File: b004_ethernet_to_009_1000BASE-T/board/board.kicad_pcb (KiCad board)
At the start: 2 copper layers, 21 x 29 mm, 8 parts, among them J1 009_1000BASE-T_2x5, J2 011_GPIO_2x3, J3 PoE_2x2, U1 7499211121A

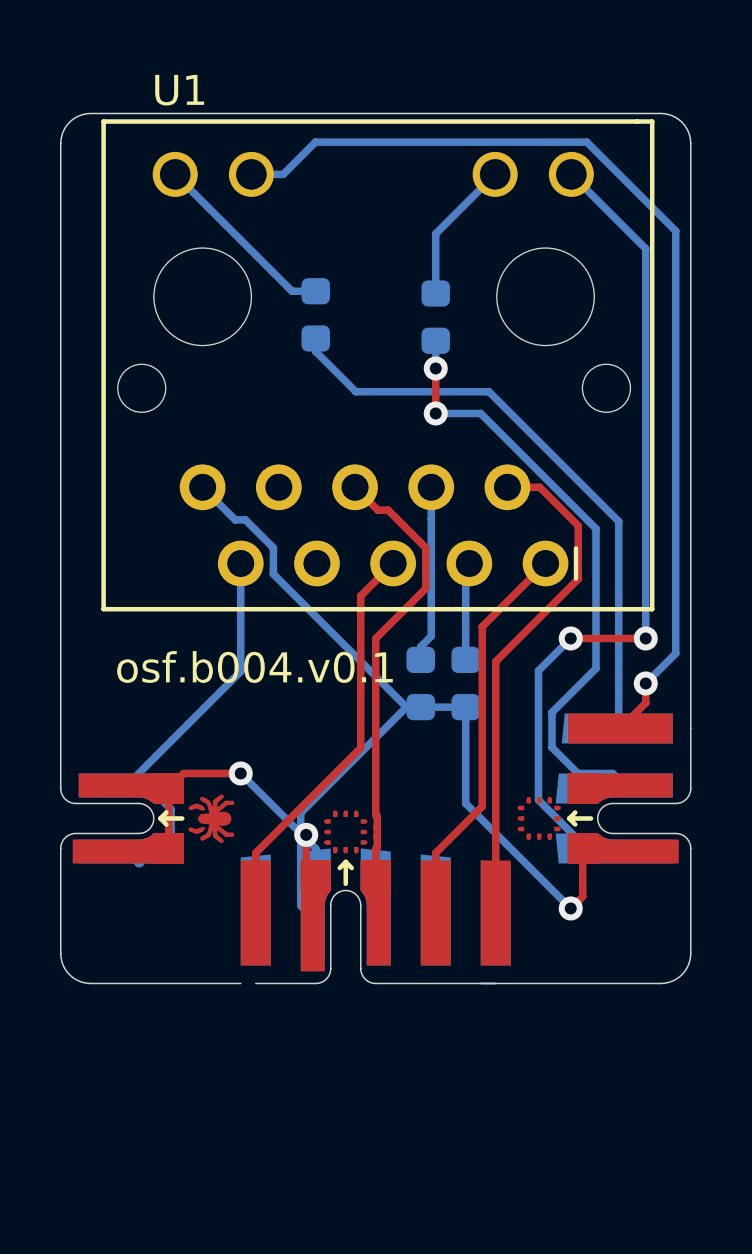
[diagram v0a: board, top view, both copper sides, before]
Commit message: added part info for silicon parts
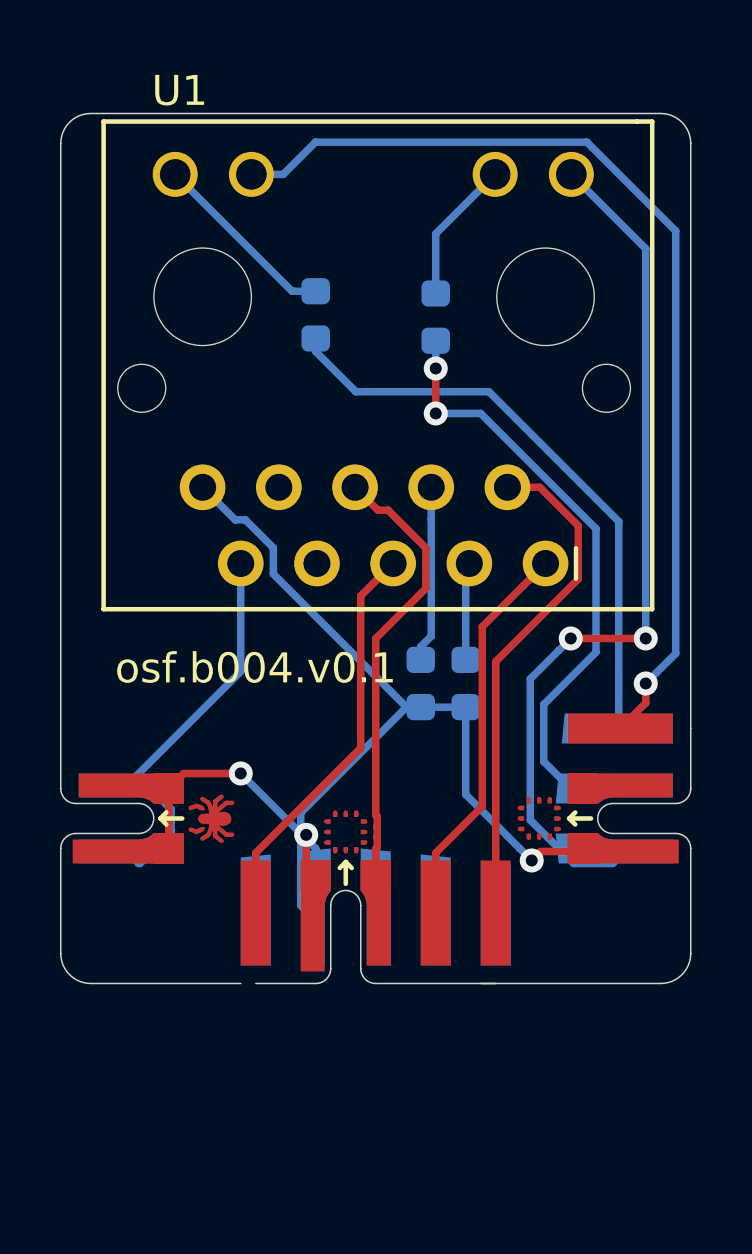
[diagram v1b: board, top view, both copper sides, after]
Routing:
- net GND: track 46.4 -> 44.0 mm
- net Net-(J2-Pad3): track 28.5 -> 29.7 mm
- net Net-(J2-Pad4): track 20.3 -> 21.0 mm
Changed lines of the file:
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@@
     (thickness 1.6)
     (drawings 12)
-    (tracks 110)
+    (tracks 113)
     (zones 0)
     (modules 8)
@@
   (gr_line (start 91 70) (end 110 70) (layer Edge.Cuts) (width 0.05))
   (segment (start 102 89.7875) (end 103.5 89.7875) (width 0.25) (layer B.Cu) (net 1))
-  (via (at 107 96.5) (size 0.8) (drill 0.4) (layers F.Cu B.Cu) (net 1))
-  (segment (start 107.4 94.5) (end 107.4 96.1) (width 0.25) (layer F.Cu) (net 1))
-  (segment (start 107.4 96.1) (end 107 96.5) (width 0.25) (layer F.Cu) (net 1))
-  (segment (start 103.5 93) (end 103.5 89.7875) (width 0.25) (layer B.Cu) (net 1))
-  (segment (start 107 96.5) (end 103.5 93) (width 0.25) (layer B.Cu) (net 1))
   (segment (start 98 93.3125) (end 101.525 89.7875) (width 0.25) (layer B.Cu) (net 1))
   (segment (start 98 96.4) (end 98 93.3125) (width 0.25) (layer B.Cu) (net 1))
@@
   (segment (start 95.817001 83.547001) (end 96.155763 83.547001) (width 0.25) (layer B.Cu) (net 1))
   (segment (start 94.73 82.46) (end 95.817001 83.547001) (width 0.25) (layer B.Cu) (net 1))
+  (via (at 105.7 94.900002) (size 0.8) (drill 0.4) (layers F.Cu B.Cu) (net 1))
+  (segment (start 103.5 89.7875) (end 103.5 92.700002) (width 0.25) (layer B.Cu) (net 1))
+  (segment (start 103.5 92.700002) (end 105.300001 94.500003) (width 0.25) (layer B.Cu) (net 1))
+  (segment (start 105.300001 94.500003) (end 105.7 94.900002) (width 0.25) (layer B.Cu) (net 1))
+  (segment (start 106.000002 94.6) (end 105.7 94.900002) (width 0.25) (layer F.Cu) (net 1))
+  (segment (start 107.4 94.5) (end 107.3 94.6) (width 0.25) (layer F.Cu) (net 1))
+  (segment (start 107.3 94.6) (end 106.000002 94.6) (width 0.25) (layer F.Cu) (net 1))
   (segment (start 100.5 94.515699) (end 100.5 95.4) (width 0.25) (layer F.Cu) (net 2))
   (segment (start 100.55001 94.134311) (end 100.55001 94.465689) (width 0.25) (layer F.Cu) (net 2))
@@
   (segment (start 104.5 88.268762) (end 104.5 96.65) (width 0.25) (layer F.Cu) (net 7))
   (segment (start 104.89 82.46) (end 105.96763 82.46) (width 0.25) (layer F.Cu) (net 7))
-  (segment (start 106.37499 89.965376) (end 107.840366 88.5) (width 0.25) (layer B.Cu) (net 8))
-  (segment (start 106.37499 91.134626) (end 106.37499 89.965376) (width 0.25) (layer B.Cu) (net 8))
-  (segment (start 107.240364 92) (end 106.37499 91.134626) (width 0.25) (layer B.Cu) (net 8))
-  (segment (start 108.9 92.5) (end 108.4 92) (width 0.25) (layer B.Cu) (net 8))
-  (segment (start 108.4 92) (end 107.240364 92) (width 0.25) (layer B.Cu) (net 8))
-  (segment (start 107.840366 88.5) (end 107.840366 83.840366) (width 0.25) (layer B.Cu) (net 8))
-  (segment (start 104 80) (end 102.5 80) (width 0.25) (layer B.Cu) (net 8))
-  (segment (start 107.840366 83.840366) (end 104 80) (width 0.25) (layer B.Cu) (net 8))
   (via (at 102.5 80) (size 0.8) (drill 0.4) (layers F.Cu B.Cu) (net 8))
   (via (at 102.5 78.5) (size 0.8) (drill 0.4) (layers F.Cu B.Cu) (net 8))
   (segment (start 102.5 80) (end 102.5 78.5) (width 0.25) (layer F.Cu) (net 8))
   (segment (start 102.5 78.5) (end 102.5 77.575) (width 0.25) (layer B.Cu) (net 8))
+  (segment (start 104 80) (end 102.5 80) (width 0.25) (layer B.Cu) (net 8))
+  (segment (start 107.840366 83.840366) (end 104 80) (width 0.25) (layer B.Cu) (net 8))
+  (segment (start 107 92.5) (end 106.1 91.6) (width 0.25) (layer B.Cu) (net 8))
+  (segment (start 108.9 92.5) (end 107 92.5) (width 0.25) (layer B.Cu) (net 8))
+  (segment (start 106.1 89.7) (end 107.840366 87.959634) (width 0.25) (layer B.Cu) (net 8))
+  (segment (start 106.1 91.6) (end 106.1 89.7) (width 0.25) (layer B.Cu) (net 8))
+  (segment (start 107.840366 87.959634) (end 107.840366 83.840366) (width 0.25) (layer B.Cu) (net 8))
   (via (at 107 87.5) (size 0.8) (drill 0.4) (layers F.Cu B.Cu) (net 9))
-  (segment (start 105.924979 88.575021) (end 107 87.5) (width 0.25) (layer B.Cu) (net 9))
-  (segment (start 105.924979 92.884615) (end 105.924979 88.575021) (width 0.25) (layer B.Cu) (net 9))
-  (segment (start 108.9 94.5) (end 107.540364 94.5) (width 0.25) (layer B.Cu) (net 9))
-  (segment (start 107.540364 94.5) (end 105.924979 92.884615) (width 0.25) (layer B.Cu) (net 9))
   (via (at 109.5 87.5) (size 0.8) (drill 0.4) (layers F.Cu B.Cu) (net 9))
   (segment (start 107 87.5) (end 109.5 87.5) (width 0.25) (layer F.Cu) (net 9))
   (segment (start 109.5 74.51) (end 107.02 72.03) (width 0.25) (layer B.Cu) (net 9))
   (segment (start 109.5 87.5) (end 109.5 74.51) (width 0.25) (layer B.Cu) (net 9))
+  (segment (start 108.9 94.5) (end 108.4 95) (width 0.25) (layer B.Cu) (net 9))
+  (segment (start 108.4 95) (end 107.1 95) (width 0.25) (layer B.Cu) (net 9))
+  (segment (start 105.649989 88.850011) (end 106.600001 87.899999) (width 0.25) (layer B.Cu) (net 9))
+  (segment (start 106.600001 87.899999) (end 107 87.5) (width 0.25) (layer B.Cu) (net 9))
+  (segment (start 107.1 95) (end 105.649989 93.549989) (width 0.25) (layer B.Cu) (net 9))
+  (segment (start 105.649989 93.549989) (end 105.649989 88.850011) (width 0.25) (layer B.Cu) (net 9))
   (segment (start 99.837498 79.274998) (end 98.5 77.9375) (width 0.25) (layer B.Cu) (net 10))
   (segment (start 98.5 77.9375) (end 98.5 77.5) (width 0.25) (layer B.Cu) (net 10))

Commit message: updated b004 to use version 0.2 connectors
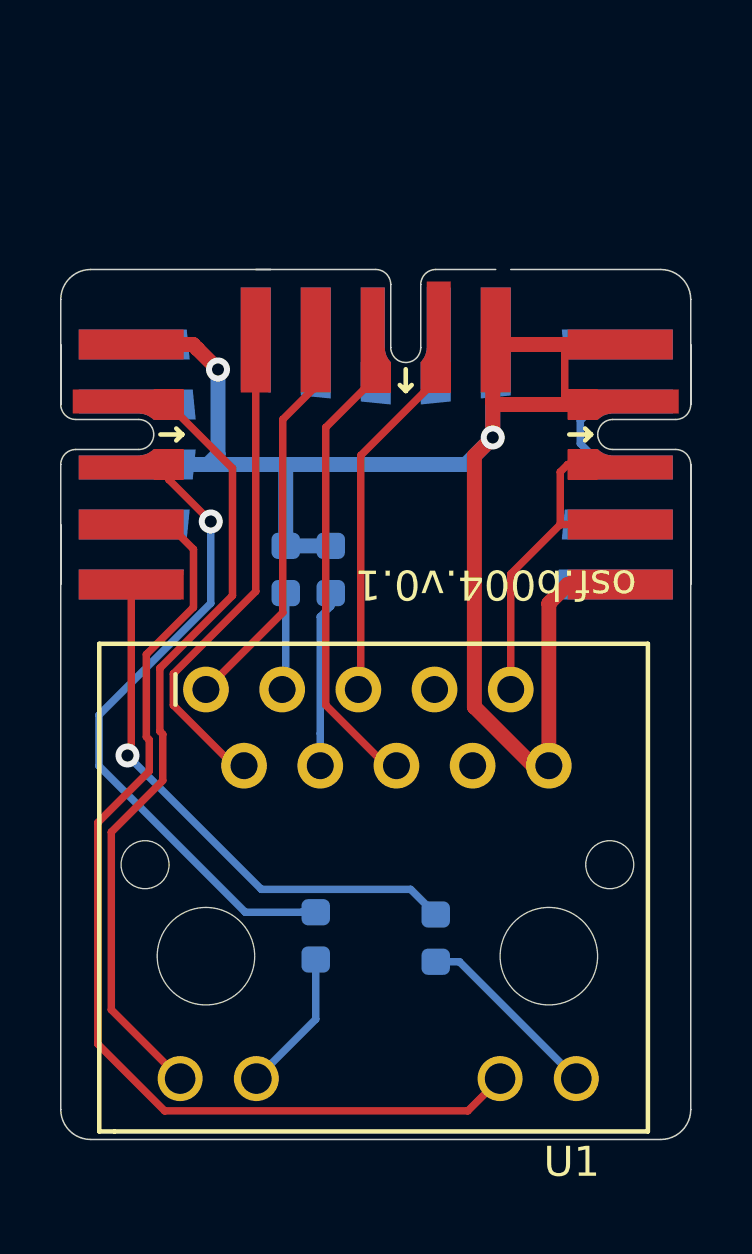
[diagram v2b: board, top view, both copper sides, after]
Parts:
- J2: footprint on_edge:on_edge_2x03_device -> on_edge:on_edge_2x05_device
- J3: footprint on_edge:on_edge_2x02_host -> on_edge:on_edge_2x05_host
- moved J1 23.8 mm to (100.5, 75.2), turned to 180 degrees
- moved J2 23.6 mm to (90.0, 81.7), turned to 270 degrees
- moved J3 23.6 mm to (111.0, 81.7), turned to 270 degrees
- moved R1 21.2 mm to (102.5, 97.5), turned to 90 degrees
- moved R2 21.0 mm to (98.5, 97.4), turned to 90 degrees
- moved U1 9.93 mm to (105.0, 89.2), turned to 180 degrees
- moved C1 7.10 mm to (97.5, 85.2), turned to 90 degrees
- moved C2 4.84 mm to (99.0, 85.2), turned to 90 degrees
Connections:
- J1 pad 3: GND -> Net-(J1-Pad3)
- J1 pad 4: (no net) -> Net-(J1-Pad4)
- J1 pad 6: (no net) -> GND
- J1 pad 7: Net-(J1-Pad7) -> (no net)
- J1 pad 9: Net-(J1-Pad9) -> (no net)
- J2 pad 2: (no net) -> Net-(J2-Pad2)
- J2 pad 6: Net-(J2-Pad6) -> (no net)
- R1 pad 2: Net-(J2-Pad6) -> Net-(J2-Pad5)
- R2 pad 2: Net-(J2-Pad4) -> Net-(J2-Pad3)
- U1 pad 1: Net-(J1-Pad5) -> Net-(J1-Pad4)
- U1 pad 11: Net-(J2-Pad3) -> Net-(J2-Pad2)
- U1 pad 13: Net-(J2-Pad5) -> Net-(J2-Pad4)
- U1 pad 2: Net-(J1-Pad9) -> Net-(J1-Pad5)
- U1 pad 5: Net-(J1-Pad7) -> Net-(J1-Pad2)
- U1 pad 6: Net-(J1-Pad2) -> Net-(J1-Pad3)
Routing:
- net Net-(J2-Pad2): track 0.00 -> 26.1 mm
- net GND: track 44.0 -> 64.8 mm, vias 3 -> 2
- net Net-(J2-Pad6): track 19.8 -> 0.00 mm
- net Net-(J1-Pad9): track 16.9 -> 0.00 mm
- net Net-(J2-Pad5): track 33.2 -> 18.2 mm
- net Net-(J1-Pad3): track 0.00 -> 14.8 mm
- net Net-(J2-Pad4): track 21.0 -> 35.1 mm, vias 2 -> 0
- net Net-(J1-Pad7): track 13.5 -> 0.00 mm
- net Net-(J1-Pad4): track 0.00 -> 13.2 mm
- net Net-(J2-Pad3): track 29.7 -> 21.4 mm, vias 2 -> 1
- net (no net): track 0.00 -> 4.69 mm
- net Net-(J1-Pad2): track 14.9 -> 11.5 mm
- net Net-(J1-Pad5): track 13.2 -> 16.5 mm
- net Net-(J3-Pad3): track 14.0 -> 10.8 mm
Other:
- outline, holes or cut-outs redrawn

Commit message: changed connector to include 100BASE-T center taps
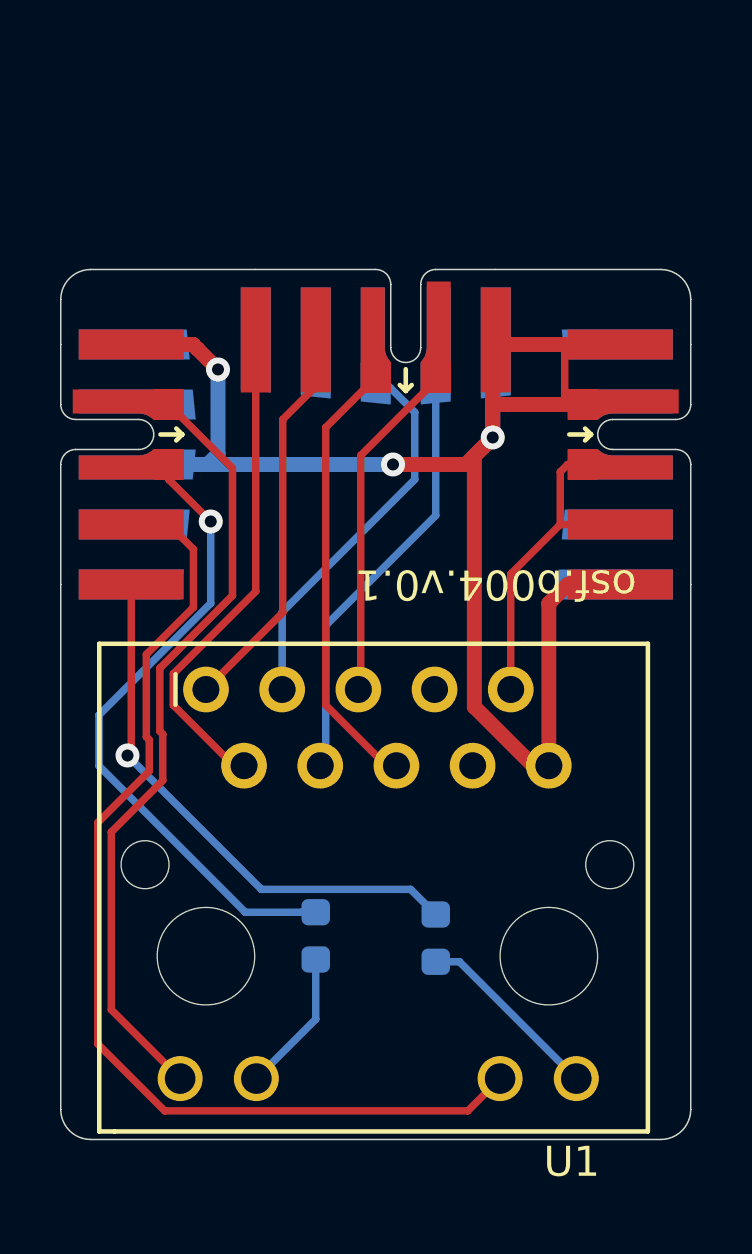
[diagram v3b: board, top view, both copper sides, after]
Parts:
- removed C1, C2: 100nF, Capacitor_SMD:C_0603_1608Metric
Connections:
- J1 pad 7: (no net) -> Net-(J1-Pad7)
- J1 pad 8: (no net) -> Net-(J1-Pad8)
- U1 pad 3: Net-(C1-Pad1) -> Net-(J1-Pad8)
- U1 pad 4: Net-(C2-Pad1) -> Net-(J1-Pad7)
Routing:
- net Net-(J1-Pad7): track 0.00 -> 16.0 mm
- net Net-(J1-Pad8): track 0.00 -> 14.3 mm
- net Net-(C2-Pad1): track 5.90 -> 0.00 mm
- net (no net): track 4.69 -> 0.00 mm
- net GND: track 64.8 -> 60.6 mm, vias 2 -> 3
- net Net-(C1-Pad1): track 3.26 -> 0.00 mm
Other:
- outline, holes or cut-outs redrawn
